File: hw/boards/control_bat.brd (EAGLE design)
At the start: 101.6 x 30.5 mm, 18 parts, among them U1 579-MCP1703T-3002ECB, U2 771-LPC824M201JDH20J, U3 888-XB24CZ7PIS-004

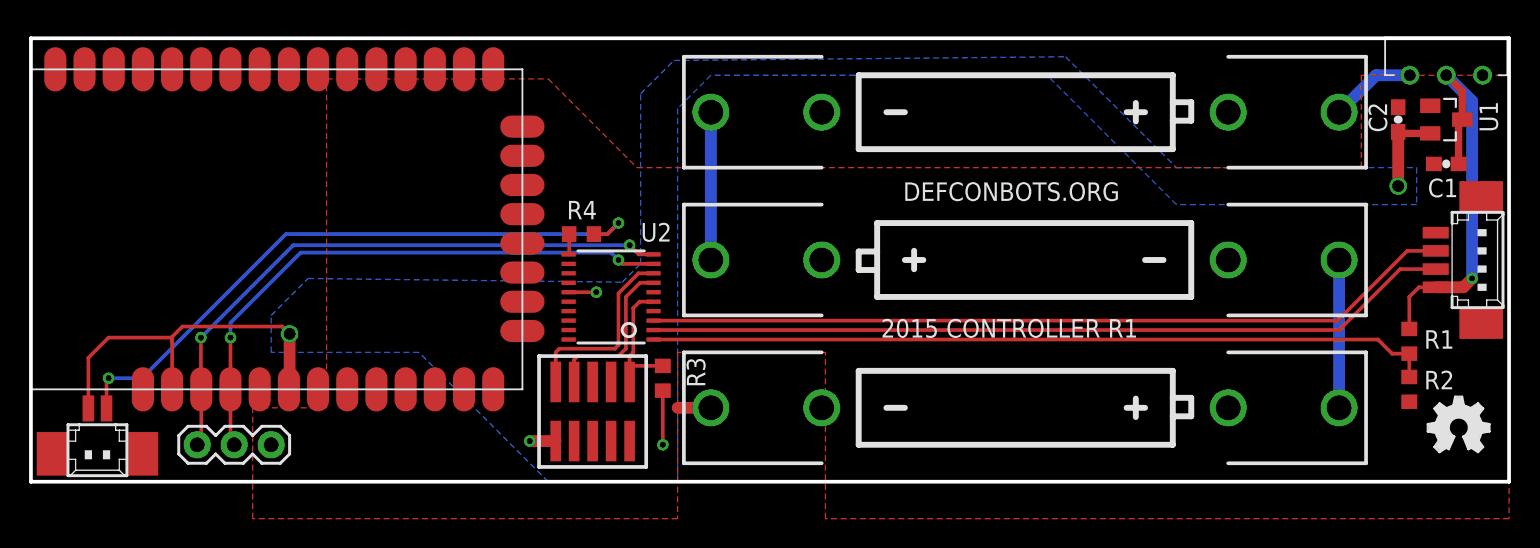
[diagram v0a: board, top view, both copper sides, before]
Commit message: Get rid of the panel, prep for proto order with dirty PCBs.
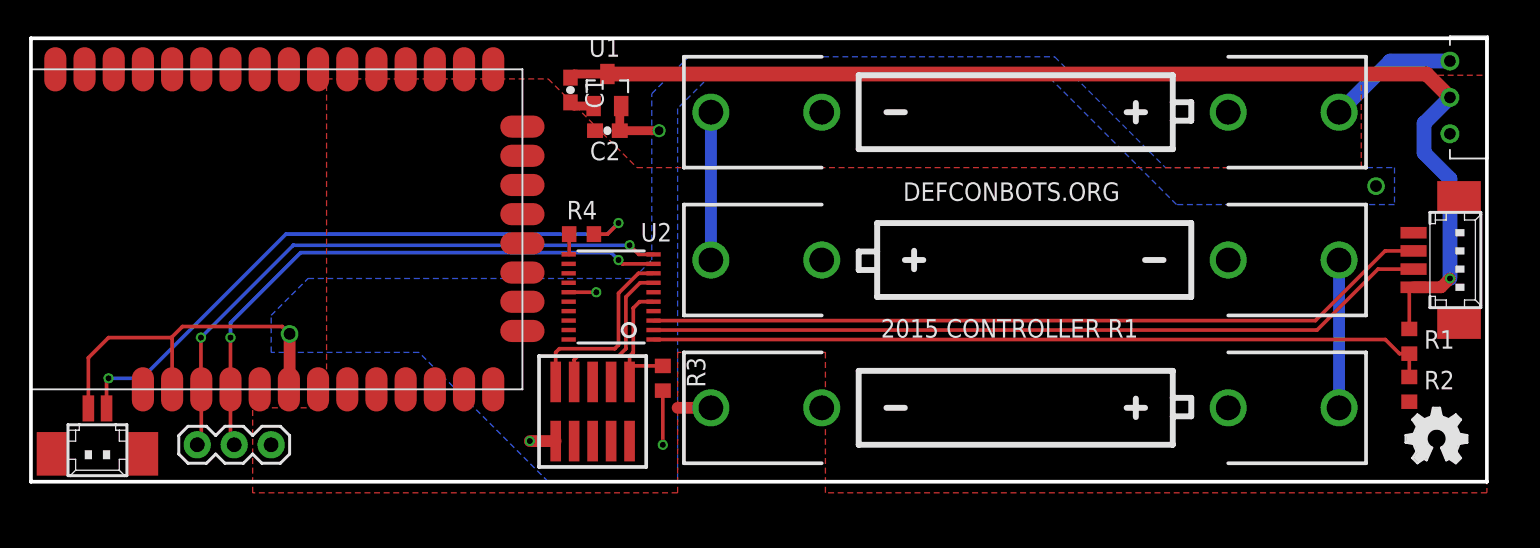
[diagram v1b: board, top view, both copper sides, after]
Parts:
- moved C1 60.4 mm to (37.1, 26.9), turned to 270 degrees
- moved U1 57.7 mm to (39.6, 26.9), turned to 0 degrees
- moved C2 54.4 mm to (39.6, 24.1), turned to 180 degrees
- moved LOGO1 1.70 mm to (94.5, 1.27)
- moved S1 1.55 mm to (97.5, 26.4), turned to 0 degrees
- moved JP3 1.52 mm to (97.5, 15.2)
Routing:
- net VIN: track 28.4 -> 81.0 mm
- net N$3: track 5.92 -> 9.08 mm
- net GND: track 2.29 -> 3.98 mm
- net +3V3: track 39.2 -> 37.7 mm, vias 5 -> 6
- net TX: track 55.5 -> 54.0 mm
- net RX: track 55.7 -> 54.2 mm
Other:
- board size 101.6 x 30.5 mm -> 100.1 x 30.5 mm
